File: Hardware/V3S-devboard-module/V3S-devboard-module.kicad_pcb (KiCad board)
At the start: 2 copper layers, 149.6 x 31.2 mm, 4 parts, among them CN1 AS0A826-H2RB-7H, J1 Bus_DDR4_Edge_Conn, J2 SODIMM DDR4 EDGE

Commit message: Started working in schematic
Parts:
- added U1: V3S, Package_QFP:LQFP-128_14x14mm_P0.4mm, F.Cu at (136.5, 93.5)
- added U2: EA3036C, Package_DFN_QFN:WQFN-20-1EP_3x3mm_P0.4mm_EP1.7x1.7mm, F.Cu at (171.5, 94.5)
- moved J2 248.6 mm to (329.3, 160.8)
- moved CN1 201.6 mm to (324.6, 110.2)
- moved J1 54.2 mm to (115.3, 110.8)
- moved R1 54.2 mm to (110.7, 104.6)
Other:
- board size 149.6 x 31.2 mm -> 283.6 x 80 mm
- board text removed: "LPDDR4 Testbed Rev. 1.2.0 12/2022"

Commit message: small improvements
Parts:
- added Y2: Crystal_GND23_Small, Crystal:Crystal_SMD_3225-4Pin_3.2x2.5mm, F.Cu at (121.8, 61.7)
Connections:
- J1 pad 11: unconnected-(J1-Pad11) -> LCD_D4
- U1 pad 1: unconnected-(U1-PG4/SDC1_D2/PG_EINT4-Pad1) -> /uP/PG4_SDCI_D2
- U1 pad 10: unconnected-(U1-PE20/CSI_FIELD/CSI_MIPI_MCLK-Pad10) -> /uP/PE20_MCSI_MCLK
- U1 pad 100: unconnected-(U1-PF6-Pad100) -> /uP/PF6
- U1 pad 101: unconnected-(U1-F5/SDC0_D2/JTAG_CK1-Pad101) -> /uP/PF5_SDC0D2_JTAGCK1
- U1 pad 102: unconnected-(U1-PF4/SDC0_D3/UART0_RX-Pad102) -> /uP/PF4_SDC0D3_UART0RX
- U1 pad 103: unconnected-(U1-PF3/SDC0_CMD/JTAG_DO1-Pad103) -> /uP/PF3_SDC0CMD_JTAGDO1
- U1 pad 104: unconnected-(U1-VCC-IO0-Pad104) -> VCC_IO
- U1 pad 105: unconnected-(U1-PF2/SDC0_CLK/UART0_TX-Pad105) -> /uP/PF2_SDC0CLK_UART0TX
- U1 pad 106: unconnected-(U1-PF1/SDC0_D0/JTAG_DI1-Pad106) -> /uP/PF1_SDC0D0_JTAGDI1
- U1 pad 107: unconnected-(U1-PF0/SDC0_D1/JTAG_MS1-Pad107) -> /uP/PF0_SDC0D1_JTAGDI1
- U1 pad 108: unconnected-(U1-VDD-SYS1-Pad108) -> VDD_SYS
- U1 pad 109: unconnected-(U1-VCC-USB-Pad109) -> VCC_USB
- U1 pad 11: unconnected-(U1-PE19/CSI_D15/LCD_D21-Pad11) -> LCD_D21
- U1 pad 110: unconnected-(U1-USB-DN-Pad110) -> /uP/USB_N
- U1 pad 111: unconnected-(U1-USB-DP-Pad111) -> /uP/USB_P
- U1 pad 112: unconnected-(U1-LRADC0-Pad112) -> /uP/LRADC0
- U1 pad 113: unconnected-(U1-MICIN1P-Pad113) -> /uP/MCIN1_P
- U1 pad 114: unconnected-(U1-MICIN1N-Pad114) -> /uP/MCIN1_N
- U1 pad 115: unconnected-(U1-AVCC-Pad115) -> AVCC
- U1 pad 116: unconnected-(U1-AGND-Pad116) -> GND
- U1 pad 117: unconnected-(U1-VRA1-Pad117) -> VRA1
- U1 pad 118: unconnected-(U1-VRA2-Pad118) -> VRA2
- U1 pad 119: unconnected-(U1-HBIAS-Pad119) -> /uP/HBIAS
- U1 pad 12: unconnected-(U1-VCC-PE0-Pad12) -> VCC_PE
- U1 pad 120: unconnected-(U1-HPOUTR-Pad120) -> /uP/HPOUTR
- U1 pad 121: unconnected-(U1-HPOUTL-Pad121) -> /uP/HPOUTL
- U1 pad 122: unconnected-(U1-HPVCCIN-Pad122) -> VCC_HP
- U1 pad 123: unconnected-(U1-HPVCCBP-Pad123) -> VCC_HP_BP
- U1 pad 124: unconnected-(U1-HPCOMFB-Pad124) -> /uP/HPCOMFB
- U1 pad 125: unconnected-(U1-HPCOM-Pad125) -> /uP/HPCOM
- U1 pad 126: unconnected-(U1-VDD-SYS2-Pad126) -> VDD_SYS
- U1 pad 127: unconnected-(U1-VCC-IO1-Pad127) -> VCC_IO
- U1 pad 128: unconnected-(U1-PG5/SDC1_D3/PG_EINT5-Pad128) -> /uP/PG5_SDCI_D3
- U1 pad 13: unconnected-(U1-PE18/CSI_D14/LCD_D20-Pad13) -> LCD_D20
- U1 pad 14: unconnected-(U1-PE17/CSI_D13/LCD_D19-Pad14) -> LCD_D19
- U1 pad 15: unconnected-(U1-PE16/CSI_D12/LCD_D18-Pad15) -> LCD_D18
- U1 pad 16: unconnected-(U1-PE15/CSI_D11/LCD_D15-Pad16) -> LCD_D15
- U1 pad 17: unconnected-(U1-PE14/CSI_D10/LCD_D14-Pad17) -> LCD_D14
- U1 pad 18: unconnected-(U1-PE13/CSI_D9/LCD_D13-Pad18) -> LCD_D13
- U1 pad 19: unconnected-(U1-VDD-SYS3-Pad19) -> VDD_SYS
- U1 pad 2: unconnected-(U1-PG3/SDC1_D1/PG_EINT3-Pad2) -> /uP/PG3_SDCI_D1
- U1 pad 20: unconnected-(U1-VDD-CPU3-Pad20) -> VDD_CPU
- U1 pad 21: unconnected-(U1-VDD-CPU2-Pad21) -> VDD_CPU
- U1 pad 22: unconnected-(U1-PE12/CSI_D8/LCD_D12-Pad22) -> LCD_D12
- U1 pad 23: unconnected-(U1-PE11/CSI_D7/LCD_D11-Pad23) -> LCD_D11
- U1 pad 24: unconnected-(U1-PE10/CSI_D6/LCD_D10-Pad24) -> LCD_D10
- U1 pad 25: unconnected-(U1-VDD-CPU1-Pad25) -> VDD_CPU
- U1 pad 26: unconnected-(U1-VDD-CPU0-Pad26) -> VDD_CPU
- U1 pad 27: unconnected-(U1-PE9/CSI_D5/LCD_D7-Pad27) -> LCD_D7
- U1 pad 28: unconnected-(U1-PE8/CSI_D4/LCD_D6-Pad28) -> LCD_D6
- U1 pad 29: unconnected-(U1-VCC-PE1-Pad29) -> VCC_PE
- U1 pad 3: unconnected-(U1-PG2/SDC1_D0/PG_EINT2-Pad3) -> /uP/PG2_SDCI_D0
- U1 pad 30: unconnected-(U1-PE7/CSI_D3/LCD_D5-Pad30) -> LCD_D5
- U1 pad 31: unconnected-(U1-PE6/CSI_D2/LCD_D4-Pad31) -> LCD_D4
- U1 pad 32: unconnected-(U1-PE5/CSI_D1/LCD_D3-Pad32) -> LCD_D3
- U1 pad 33: unconnected-(U1-PE4/CSI_D0/LCD_D2-Pad33) -> LCD_D2
- U1 pad 34: unconnected-(U1-PE3/CSI_VSYNC/LCD_VSYNC-Pad34) -> /uP/LCD_VSYNC
- U1 pad 35: unconnected-(U1-PE2/CSI_HSYNC/LCD_HSYNC-Pad35) -> /uP/LCD_HSYNC
- U1 pad 36: unconnected-(U1-PE1/CSI_MCLK/LCD_DE-Pad36) -> /uP/LCD_DE
- U1 pad 37: unconnected-(U1-PE0/CSI_PCLK/LCD_CLK-Pad37) -> /uP/LCD_CLK
- U1 pad 38: unconnected-(U1-VDD-CPU4-Pad38) -> VDD_CPU
- U1 pad 39: unconnected-(U1-PB0/UART2_TX/PB_EINT0-Pad39) -> /uP/PB0_UART2TX
- U1 pad 4: unconnected-(U1-PG1/SDC1_CMD/PG_EINT1-Pad4) -> /uP/PG0_MCSI_PDWN
- U1 pad 40: unconnected-(U1-PB1/UART2_RX/PB_EINT1-Pad40) -> /uP/PB1_UART2RX
- U1 pad 41: unconnected-(U1-PB2/UART2_RTS/PB_EINT2-Pad41) -> /uP/PB2_UART2RTS
- U1 pad 42: unconnected-(U1-PB3/UART2_CTS/PB_EINT3-Pad42) -> /uP/PB3_UART2CTS
- U1 pad 43: unconnected-(U1-PB4/PWM0/PB_EINT4-Pad43) -> /uP/PB4_PWM0
- U1 pad 44: unconnected-(U1-PB5/PWM1/PB_EINT5-Pad44) -> /uP/PB5_PWM1
- U1 pad 45: unconnected-(U1-PB6/TWI0_SCK/PB_EINT6-Pad45) -> /uP/PB6_SCK
- U1 pad 46: unconnected-(U1-PB7/TWI0_SDA/PB_EINT7-Pad46) -> /uP/PB7_SDA
- U1 pad 47: unconnected-(U1-VDD-CPU5-Pad47) -> VDD_CPU
- U1 pad 48: unconnected-(U1-PB8/TWI1_SCK/UART0_TX/PB_EINT8-Pad48) -> /uP/PB8_SCK_UART0TX
- U1 pad 49: unconnected-(U1-PB9/TWI1_SDA/UART0_RX/PB_EINT9-Pad49) -> /uP/PB9_SDA_UART0RX
- U1 pad 5: unconnected-(U1-PG0/SDC1_CLK/PG_EINT0-Pad5) -> /uP/PG0_MCSI_RST
- U1 pad 50: unconnected-(U1-VCC-IO3-Pad50) -> VCC_IO
- U1 pad 51: unconnected-(U1-VDD-CPU6-Pad51) -> VDD_CPU
- U1 pad 52: unconnected-(U1-PC0/SDC2_CLK/SPI_MISO-Pad52) -> /uP/PC0_SPI_MISO
- U1 pad 53: unconnected-(U1-PC1/SDC2_CMD/SPI_CLK-Pad53) -> /uP/PC1_SPI_CLK
- U1 pad 54: unconnected-(U1-PC2/SDC2_RST/SPI_CS-Pad54) -> /uP/PC2_SPI_CS
- U1 pad 55: unconnected-(U1-PC3/SDC2_D0/SPI_MOSI-Pad55) -> /uP/PC3_SPI_MOSI
- U1 pad 56: unconnected-(U1-VDD-CPU7-Pad56) -> VDD_CPU
- U1 pad 57: unconnected-(U1-VCC-IO2-Pad57) -> VCC_IO
- U1 pad 58: unconnected-(U1-VDD-SYS4-Pad58) -> VDD_SYS
- U1 pad 59: unconnected-(U1-VCC-DRAM8-Pad59) -> VCC_DRAM
- U1 pad 6: unconnected-(U1-PE24/LCD_D23-Pad6) -> LCD_D23
- U1 pad 60: unconnected-(U1-VCC-DRAM9-Pad60) -> VCC_DRAM
- U1 pad 61: unconnected-(U1-VCC-DRAM10-Pad61) -> VCC_DRAM
- U1 pad 62: unconnected-(U1-VCC-DARM11-Pad62) -> VCC_DRAM
- U1 pad 63: unconnected-(U1-SVREF1-Pad63) -> SVREF
- U1 pad 64: unconnected-(U1-VDD-SYS5-Pad64) -> VDD_SYS
- U1 pad 65: unconnected-(U1-VCC-DRAM0-Pad65) -> VCC_DRAM
- U1 pad 66: unconnected-(U1-VCC-DRAM1-Pad66) -> VCC_DRAM
- U1 pad 67: unconnected-(U1-VCC-DRAM2-Pad67) -> VCC_DRAM
- U1 pad 68: unconnected-(U1-VCC-DRAM3-Pad68) -> VCC_DRAM
- U1 pad 69: unconnected-(U1-VCC-DRAM4-Pad69) -> VCC_DRAM
- U1 pad 7: unconnected-(U1-PE23/LCD_D22-Pad7) -> LCD_D22
- U1 pad 70: unconnected-(U1-VCC-DRAM5-Pad70) -> VCC_DRAM
- U1 pad 71: unconnected-(U1-SVREF0-Pad71) -> SVREF
- U1 pad 72: unconnected-(U1-VCC-DRAM6-Pad72) -> VCC_DRAM
- U1 pad 73: unconnected-(U1-SZQ-Pad73) -> /uP/SZQ
- U1 pad 74: unconnected-(U1-X24MOUT-Pad74) -> /uP/X24MOUT
- U1 pad 75: unconnected-(U1-X24MIN-Pad75) -> /uP/X24_MIN
- U1 pad 76: unconnected-(U1-VCC-PLL-Pad76) -> VCC_PLL
- U1 pad 77: unconnected-(U1-EPHY-LINK-LED-Pad77) -> /uP/ETH_LED_LINK
- U1 pad 78: unconnected-(U1-EPHY-SPD-LED-Pad78) -> /uP/ETH_LED_SPD
- U1 pad 79: unconnected-(U1-VCC-DRAM7-Pad79) -> VCC_DRAM
- U1 pad 8: unconnected-(U1-PE22/CSI_SDA/TWI1_SDA/UART1_RX-Pad8) -> /uP/PE22_CSI_SDA
- U1 pad 80: unconnected-(U1-VDD-SYS0-Pad80) -> VDD_SYS
- U1 pad 81: unconnected-(U1-MCSI-D0P-Pad81) -> /uP/MSCI_D0_P
- U1 pad 82: unconnected-(U1-MCSI-D0N-Pad82) -> /uP/MSCI_D0_N
- U1 pad 83: unconnected-(U1-MCSI-D1P-Pad83) -> /uP/MSCI_D1_P
- U1 pad 84: unconnected-(U1-MCSI-D1N-Pad84) -> /uP/MSCI_D1_N
- U1 pad 85: unconnected-(U1-VCC-MCSI-Pad85) -> VCC_MSCI
- U1 pad 86: unconnected-(U1-MCSI-CKP-Pad86) -> /uP/MSCI_CLK_P
- U1 pad 87: unconnected-(U1-MCSI-CKN-Pad87) -> /uP/MSCI_CLK_N
- U1 pad 88: unconnected-(U1-EPHY-VDD-Pad88) -> VDD_PHY
- U1 pad 89: unconnected-(U1-EPHY-RXN-Pad89) -> ETH0.RX_N
- U1 pad 9: unconnected-(U1-PE21/CSI_SCK/TWI1_SCK/UART1_TX-Pad9) -> /uP/PE21_CSI_SCK
- U1 pad 90: unconnected-(U1-EPHY-RXP-Pad90) -> ETH0.RX_P
- U1 pad 91: unconnected-(U1-EPHY-TXN-Pad91) -> ETH0.TX_N
- U1 pad 92: unconnected-(U1-EPHY-TXP-Pad92) -> ETH0.TX_P
- U1 pad 93: unconnected-(U1-EPHY-VCC-Pad93) -> VCC_PHY
- U1 pad 94: unconnected-(U1-EPHY-RTX-Pad94) -> Net-(U1-EPHY-RTX)
- U1 pad 95: unconnected-(U1-X32KOUT-Pad95) -> /uP/X32KOUT
- U1 pad 96: unconnected-(U1-X32KIN-Pad96) -> /uP/X32KIN
- U1 pad 97: unconnected-(U1-RTC-VIO-Pad97) -> VCC_RTCIO
- U1 pad 98: unconnected-(U1-VCC-RTC-Pad98) -> VCC_RTC
- U1 pad 99: unconnected-(U1-RESET-Pad99) -> /uP/RESET

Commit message: schematic improvements
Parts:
- added REF**: CONN-SMD_AS0BC21-S30BE-7H, v3s-devboard-module:CONN-SMD_AS0BC21-S30BE-7H, F.Cu at (33.1, 167.9)
- added REF**: m2-padKeyE, v3s-devboard-module:m2-padKeyE, B.Cu at (64.7, 184.9)
- added U$3: M.2-B-KEY-2280-ADAPTER, M.2-Templates:M.2-B-KEY-2280-ADAPTER, F.Cu at (222.9, 152.2)
- moved U1 113.1 mm to (34.1, 141.5), turned to 45 degrees
- moved U2 1.33 mm to (171.2, 93.2)

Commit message: general improvements. power almost complete
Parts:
- removed CN1: AS0A826-H2RB-7H, SODIMM:SODIMM_DDR4_EDGE
- removed R1: R_US, Resistor_SMD:R_0402_1005Metric_Pad0.72x0.64mm_HandSolder
- removed U$3: M.2-B-KEY-2280-ADAPTER, M.2-Templates:M.2-B-KEY-2280-ADAPTER
- added CN3: AS0BC21-S30BE-7H, v3s-devboard-module:m2-padKeyE, F.Cu at (89.8, 102.9)
- added RN1: 6x47K, Resistor_THT:R_Array_SIP7, F.Cu at (36.5, 97.5)
- added U3: XC6206PxxxMR, Package_TO_SOT_SMD:SOT-23-3, F.Cu at (58.5, 97.7)
- added U4: W25Q128JVS, Package_SO:SOIC-8_5.23x5.23mm_P1.27mm, F.Cu at (39.4, 119.4)
- added U5: AP3019AKTR-G1, Package_TO_SOT_SMD:SOT-23-6, F.Cu at (47.2, 118.4)
- J2: value SODIMM DDR4 EDGE -> Micro_SD_Card_Det1; footprint SODIMM:SODIMM_DDR4_EDGE -> v3s-devboard-module:J_sd_micro_socket
- U1: footprint Package_QFP:LQFP-128_14x14mm_P0.4mm -> v3s-devboard-module:LQFP-128_L14.0-W14.0-P0.40-LS16.0-BL-EP5.0
- moved J2 290.2 mm to (44.1, 107.7)
- moved U1 99.7 mm to (123.4, 97.2)
- moved REF** 88.6 mm to (89.8, 99.8)
- moved J1 86.1 mm to (32.2, 88.4)
- moved REF** 84.0 mm to (121.0, 122.6)
- moved U2 55.3 mm to (118.2, 77.6)
- moved Y2 16.8 mm to (128.1, 77.2)
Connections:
- net VCC_DRAM renamed 1V8
- J2 pad 1: (no net) -> /uP/PF5_SDC0D2_JTAGCK1
- J2 pad 2: (no net) -> /uP/PF4_SDC0D3_UART0RX
- J2 pad 3: (no net) -> /uP/PF3_SDC0CMD_JTAGDO1
- J2 pad 4: (no net) -> 3V3
- J2 pad 5: (no net) -> /uP/PF2_SDC0CLK_UART0TX
- J2 pad 6: (no net) -> GND
- J2 pad 7: (no net) -> /uP/PF1_SDC0D0_JTAGDI1
- J2 pad 8: (no net) -> /uP/PF0_SDC0D1_JTAGDI1
- J2 pad 9: (no net) -> /uP/PF6
- U1 pad 10: /uP/PE20_MCSI_MCLK -> CSI.MCSI_MCLK
- U1 pad 104: VCC_IO -> 3V3
- U1 pad 108: VDD_SYS -> 1V2
- U1 pad 109: VCC_USB -> 3V3
- U1 pad 115: AVCC -> 3V0
- U1 pad 12: VCC_PE -> 3V3
- U1 pad 122: VCC_HP -> 3V3
- U1 pad 126: VDD_SYS -> 1V2
- U1 pad 127: VCC_IO -> 3V3
- U1 pad 19: VDD_SYS -> 1V2
- U1 pad 20: VDD_CPU -> 1V2
- U1 pad 21: VDD_CPU -> 1V2
- U1 pad 25: VDD_CPU -> 1V2
- U1 pad 26: VDD_CPU -> 1V2
- U1 pad 29: VCC_PE -> 3V3
- U1 pad 34: /uP/LCD_VSYNC -> LCD0.VSYNC
- U1 pad 35: /uP/LCD_HSYNC -> LCD0.HSYNC
- U1 pad 36: /uP/LCD_DE -> LCD0.DE
- U1 pad 37: /uP/LCD_CLK -> LCD0.CLK
- U1 pad 38: VDD_CPU -> 1V2
- U1 pad 39: /uP/PB0_UART2TX -> UART2.TX
- U1 pad 40: /uP/PB1_UART2RX -> UART2.RX
- U1 pad 41: /uP/PB2_UART2RTS -> /uP/PB2
- U1 pad 42: /uP/PB3_UART2CTS -> UART2.CTS
- U1 pad 47: VDD_CPU -> 1V2
- U1 pad 48: /uP/PB8_SCK_UART0TX -> UART0.TX
- U1 pad 49: /uP/PB9_SDA_UART0RX -> UART0.RX
- U1 pad 50: VCC_IO -> 3V3
- U1 pad 51: VDD_CPU -> 1V2
- U1 pad 52: /uP/PC0_SPI_MISO -> SPI.MISO
- U1 pad 53: /uP/PC1_SPI_CLK -> SPI.CLK
- U1 pad 54: /uP/PC2_SPI_CS -> SPI.CS
- U1 pad 55: /uP/PC3_SPI_MOSI -> SPI.MOSI
- U1 pad 56: VDD_CPU -> 1V2
- U1 pad 57: VCC_IO -> 3V3
- U1 pad 58: VDD_SYS -> 1V2
- U1 pad 64: VDD_SYS -> 1V2
- U1 pad 76: VCC_PLL -> 3V0
- U1 pad 77: /uP/ETH_LED_LINK -> ETH_LED_LINK
- U1 pad 78: /uP/ETH_LED_SPD -> ETH_LED_SPD
- U1 pad 8: /uP/PE22_CSI_SDA -> CSI.CSI_SDA
- U1 pad 80: VDD_SYS -> 1V2
- U1 pad 81: /uP/MSCI_D0_P -> CSI.MCSI_D0_P
- U1 pad 82: /uP/MSCI_D0_N -> CSI.MCSI_D0_N
- U1 pad 83: /uP/MSCI_D1_P -> CSI.MCSI_D1_P
- U1 pad 84: /uP/MSCI_D1_N -> CSI.MCSI_D1_N
- U1 pad 85: VCC_MSCI -> 3V3
- U1 pad 86: /uP/MSCI_CLK_P -> CSI.MCSI_CK_P
- U1 pad 87: /uP/MSCI_CLK_N -> CSI.MCSI_CK_N
- U1 pad 88: VDD_PHY -> 1V2
- U1 pad 9: /uP/PE21_CSI_SCK -> CSI.CSI_SCK
- U1 pad 93: VCC_PHY -> 3V3
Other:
- board size 283.6 x 80 mm -> 69.6 x 26 mm

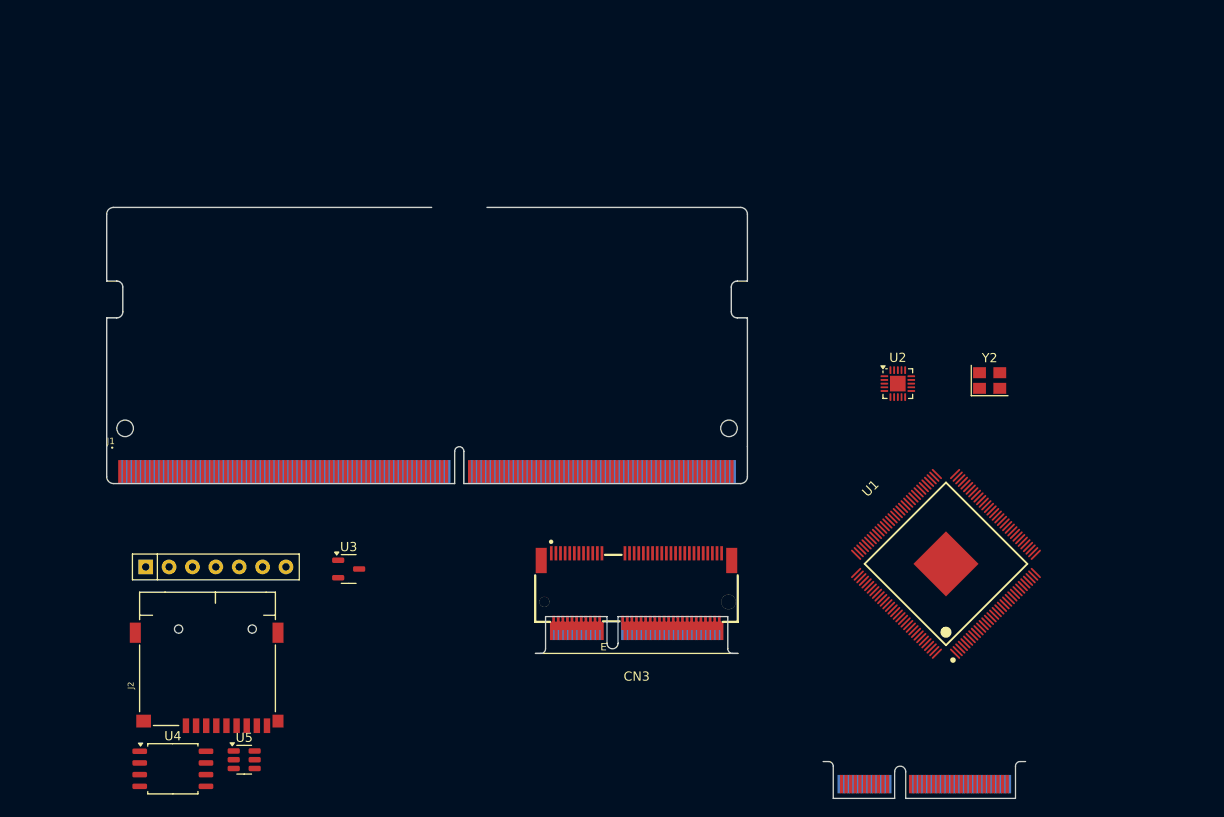
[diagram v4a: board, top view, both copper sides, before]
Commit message: fixed minor schematic issues
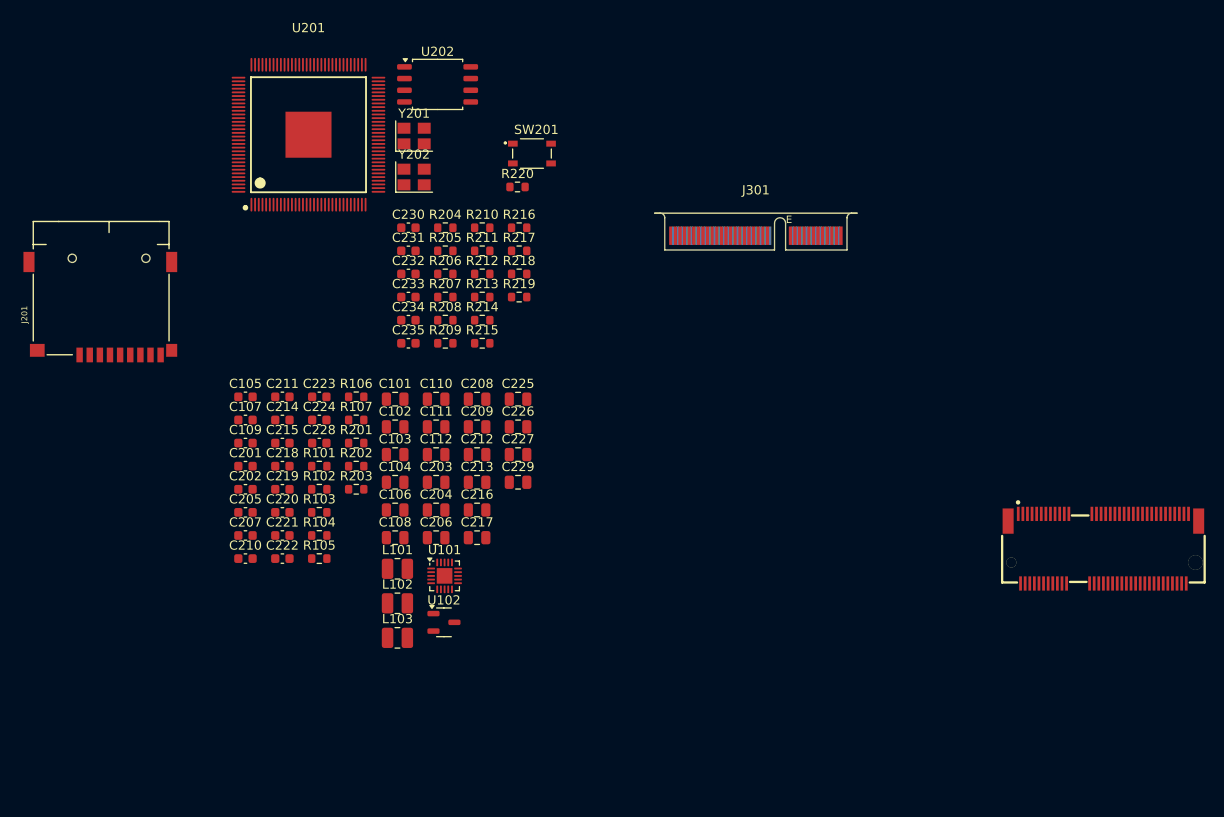
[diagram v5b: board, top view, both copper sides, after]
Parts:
- removed CN3: AS0BC21-S30BE-7H, v3s-devboard-module:m2-padKeyE
- removed J1: Bus_DDR4_Edge_Conn, SODIMM-DDR4:Bus_DDR4_Conn_Edge
- removed J2: Micro_SD_Card_Det1, v3s-devboard-module:J_sd_micro_socket
- removed the REF** at (121.0, 122.6)
- removed RN1: 6x47K, Resistor_THT:R_Array_SIP7
- removed U1: V3S, v3s-devboard-module:LQFP-128_L14.0-W14.0-P0.40-LS16.0-BL-EP5.0
- removed U2: EA3036C, Package_DFN_QFN:WQFN-20-1EP_3x3mm_P0.4mm_EP1.7x1.7mm
- removed U3: XC6206PxxxMR, Package_TO_SOT_SMD:SOT-23-3
- removed U4: W25Q128JVS, Package_SO:SOIC-8_5.23x5.23mm_P1.27mm
- removed U5: AP3019AKTR-G1, Package_TO_SOT_SMD:SOT-23-6
- removed Y2: Crystal_GND23_Small, Crystal:Crystal_SMD_3225-4Pin_3.2x2.5mm
- added C101: 1u, Capacitor_SMD:C_0805_2012Metric, F.Cu at (63.6, 79.3)
- added C102: 10u, Capacitor_SMD:C_0805_2012Metric, F.Cu at (63.6, 82.3)
- added C103: 10u, Capacitor_SMD:C_0805_2012Metric, F.Cu at (63.6, 85.3)
- added C104: 10u, Capacitor_SMD:C_0805_2012Metric, F.Cu at (63.6, 88.3)
- added C105: 18p, Capacitor_SMD:C_0603_1608Metric, F.Cu at (47.3, 79.0)
- added C106: 10u, Capacitor_SMD:C_0805_2012Metric, F.Cu at (63.6, 91.3)
- added C107: 18p, Capacitor_SMD:C_0603_1608Metric, F.Cu at (47.3, 81.5)
- added C108: 10u, Capacitor_SMD:C_0805_2012Metric, F.Cu at (63.6, 94.3)
- added C109: 18p, Capacitor_SMD:C_0603_1608Metric, F.Cu at (47.3, 84.0)
- added C110: 10u, Capacitor_SMD:C_0805_2012Metric, F.Cu at (68.0, 79.3)
- added C111: 1u, Capacitor_SMD:C_0805_2012Metric, F.Cu at (68.0, 82.3)
- added C112: 1u, Capacitor_SMD:C_0805_2012Metric, F.Cu at (68.0, 85.3)
- added C201: 100n, Capacitor_SMD:C_0603_1608Metric, F.Cu at (47.3, 86.5)
- added C202: 100n, Capacitor_SMD:C_0603_1608Metric, F.Cu at (47.3, 89.0)
- added C203: 10u, Capacitor_SMD:C_0805_2012Metric, F.Cu at (68.0, 88.3)
- added C204: 1u, Capacitor_SMD:C_0805_2012Metric, F.Cu at (68.0, 91.3)
- added C205: 100n, Capacitor_SMD:C_0603_1608Metric, F.Cu at (47.3, 91.6)
- added C206: 1u, Capacitor_SMD:C_0805_2012Metric, F.Cu at (68.0, 94.3)
- added C207: 100n, Capacitor_SMD:C_0603_1608Metric, F.Cu at (47.3, 94.1)
- added C208: 10u, Capacitor_SMD:C_0805_2012Metric, F.Cu at (72.5, 79.3)
- added C209: 1u, Capacitor_SMD:C_0805_2012Metric, F.Cu at (72.5, 82.3)
- added C210: 100n, Capacitor_SMD:C_0603_1608Metric, F.Cu at (47.3, 96.6)
- added C211: 100n, Capacitor_SMD:C_0603_1608Metric, F.Cu at (51.3, 79.0)
- added C212: 10u, Capacitor_SMD:C_0805_2012Metric, F.Cu at (72.5, 85.3)
- added C213: 1u, Capacitor_SMD:C_0805_2012Metric, F.Cu at (72.5, 88.3)
- added C214: 100n, Capacitor_SMD:C_0603_1608Metric, F.Cu at (51.3, 81.5)
- added C215: 100n, Capacitor_SMD:C_0603_1608Metric, F.Cu at (51.3, 84.0)
- added C216: 10u, Capacitor_SMD:C_0805_2012Metric, F.Cu at (72.5, 91.3)
- added C217: 1u, Capacitor_SMD:C_0805_2012Metric, F.Cu at (72.5, 94.3)
- added C218: 100n, Capacitor_SMD:C_0603_1608Metric, F.Cu at (51.3, 86.5)
- added C219: 100n, Capacitor_SMD:C_0603_1608Metric, F.Cu at (51.3, 89.0)
- added C220: 100n, Capacitor_SMD:C_0603_1608Metric, F.Cu at (51.3, 91.6)
- added C221: 100n, Capacitor_SMD:C_0603_1608Metric, F.Cu at (51.3, 94.1)
- added C222: 100n, Capacitor_SMD:C_0603_1608Metric, F.Cu at (51.3, 96.6)
- added C223: 100n, Capacitor_SMD:C_0603_1608Metric, F.Cu at (55.3, 79.0)
- added C224: 100n, Capacitor_SMD:C_0603_1608Metric, F.Cu at (55.3, 81.5)
- added C225: 1u, Capacitor_SMD:C_0805_2012Metric, F.Cu at (76.9, 79.3)
- added C226: 4.7u, Capacitor_SMD:C_0805_2012Metric, F.Cu at (76.9, 82.3)
- added C227: 10u, Capacitor_SMD:C_0805_2012Metric, F.Cu at (76.9, 85.3)
- added C228: 100n, Capacitor_SMD:C_0603_1608Metric, F.Cu at (55.3, 84.0)
- added C229: 4.7u, Capacitor_SMD:C_0805_2012Metric, F.Cu at (76.9, 88.3)
- added C230: 18p, Capacitor_SMD:C_0603_1608Metric, F.Cu at (65.0, 60.6)
- added C231: 18p, Capacitor_SMD:C_0603_1608Metric, F.Cu at (65.0, 63.1)
- added C232: 18p, Capacitor_SMD:C_0603_1608Metric, F.Cu at (65.0, 65.7)
- added C233: 18p, Capacitor_SMD:C_0603_1608Metric, F.Cu at (65.0, 68.2)
- added C234: 1u, Capacitor_SMD:C_0603_1608Metric, F.Cu at (65.0, 70.7)
- added C235: 100n, Capacitor_SMD:C_0603_1608Metric, F.Cu at (65.0, 73.2)
- added J201: Micro_SD_Card_Det1, v3s-devboard-module:J_sd_micro_socket, F.Cu at (32.5, 67.4)
- added J301: AS0BC21-S30BE-7H, v3s-devboard-module:m2-padKeyE, F.Cu at (102.8, 63.0)
- added L101: 2.2u, Inductor_SMD:L_1008_2520Metric, F.Cu at (63.8, 97.7)
- added L102: 2.2u, Inductor_SMD:L_1008_2520Metric, F.Cu at (63.8, 101.4)
- added L103: 2.2u, Inductor_SMD:L_1008_2520Metric, F.Cu at (63.8, 105.2)
- added R101: 150K, Resistor_SMD:R_0603_1608Metric, F.Cu at (55.3, 86.5)
- added R102: 150K, Resistor_SMD:R_0603_1608Metric, F.Cu at (55.3, 89.0)
- added R103: 200K, Resistor_SMD:R_0603_1608Metric, F.Cu at (55.3, 91.6)
- added R104: 100K, Resistor_SMD:R_0603_1608Metric, F.Cu at (55.3, 94.1)
- added R105: 680K, Resistor_SMD:R_0603_1608Metric, F.Cu at (55.3, 96.6)
- added R106: 150K, Resistor_SMD:R_0603_1608Metric, F.Cu at (59.3, 79.0)
- added R107: 0, Resistor_SMD:R_0603_1608Metric, F.Cu at (59.3, 81.5)
- added R201: 2K, Resistor_SMD:R_0603_1608Metric, F.Cu at (59.3, 84.0)
- added R202: 2K, Resistor_SMD:R_0603_1608Metric, F.Cu at (59.3, 86.5)
- added R203: 200K, Resistor_SMD:R_0603_1608Metric, F.Cu at (59.3, 89.0)
- added R204: 10M, Resistor_SMD:R_0603_1608Metric, F.Cu at (69.0, 60.6)
- added R205: 10M, Resistor_SMD:R_0603_1608Metric, F.Cu at (69.0, 63.1)
- added R206: 240, Resistor_SMD:R_0603_1608Metric, F.Cu at (69.0, 65.7)
- added R207: 47K, Resistor_SMD:R_0603_1608Metric, F.Cu at (69.0, 68.2)
- added R208: 10K, Resistor_SMD:R_0603_1608Metric, F.Cu at (69.0, 70.7)
- added R209: 33, Resistor_SMD:R_0603_1608Metric, F.Cu at (69.0, 73.2)
- added R210: 47K, Resistor_SMD:R_0603_1608Metric, F.Cu at (73.0, 60.6)
- added R211: 10k, Resistor_SMD:R_0603_1608Metric, F.Cu at (73.0, 63.1)
- added R212: 10k, Resistor_SMD:R_0603_1608Metric, F.Cu at (73.0, 65.7)
- added R213: 10k, Resistor_SMD:R_0603_1608Metric, F.Cu at (73.0, 68.2)
- added R214: 10k, Resistor_SMD:R_0603_1608Metric, F.Cu at (73.0, 70.7)
- added R215: 10k, Resistor_SMD:R_0603_1608Metric, F.Cu at (73.0, 73.2)
- added R216: 33, Resistor_SMD:R_0603_1608Metric, F.Cu at (77.0, 60.6)
- added R217: 33, Resistor_SMD:R_0603_1608Metric, F.Cu at (77.0, 63.1)
- added R218: 33, Resistor_SMD:R_0603_1608Metric, F.Cu at (77.0, 65.7)
- added R219: 33, Resistor_SMD:R_0603_1608Metric, F.Cu at (77.0, 68.2)
- added R220: 6K, Resistor_SMD:R_0603_1608Metric, F.Cu at (76.9, 56.2)
- added SW201: SW_MEC_5E, v3s-devboard-module:SW_SKRPACE010, F.Cu at (78.4, 52.6)
- added U101: EA3036C, Package_DFN_QFN:WQFN-20-1EP_3x3mm_P0.4mm_EP1.7x1.7mm, F.Cu at (68.9, 98.5)
- added U102: XC6206PxxxMR, Package_TO_SOT_SMD:SOT-23-3, F.Cu at (68.9, 103.5)
- added U201: V3S, v3s-devboard-module:LQFP-128_L14.0-W14.0-P0.40-LS16.0-BL-EP5.0, F.Cu at (54.1, 50.5)
- added U202: W25Q128JVS, Package_SO:SOIC-8_5.23x5.23mm_P1.27mm, F.Cu at (68.2, 45.1)
- added Y201: Crystal_GND23_Small, Crystal:Crystal_SMD_3225-4Pin_3.2x2.5mm, F.Cu at (65.6, 50.7)
- added Y202: Crystal_GND23_Small, Crystal:Crystal_SMD_3225-4Pin_3.2x2.5mm, F.Cu at (65.6, 55.1)
- moved REF** 50.9 mm to (140.5, 95.5)
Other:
- board size 69.6 x 26 mm -> 22 x 4 mm

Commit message: started preparing layout
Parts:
- C220, C221, C227, C228: moved to B.Cu
- moved C202 137.3 mm to (168.5, 24.5), turned to 90 degrees
- moved C201 133.9 mm to (166.0, 24.5), turned to 90 degrees
- moved C207 132.2 mm to (159.3, 23.8)
- moved C210 131.1 mm to (173.7, 62.0)
- moved C205 128.4 mm to (159.4, 29.0)
- moved R202 123.9 mm to (168.5, 28.0), turned to 90 degrees
- moved C211 123.0 mm to (173.7, 66.5)
- moved C218 122.9 mm to (164.0, 37.5)
- moved C219 122.9 mm to (164.0, 40.0)
- moved R201 121.4 mm to (167.0, 28.0), turned to 90 degrees
- moved C220 120.7 mm to (158.8, 36.5), turned to 180 degrees
- moved C206 116.6 mm to (159.5, 22.0)
- moved C204 111.8 mm to (159.4, 27.0)
- moved C221 111.6 mm to (153.0, 48.0), turned to 90 degrees
- moved C216 110.5 mm to (169.0, 37.5)
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
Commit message: layout improvements.
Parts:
- added NT1: NetTie_2, NetTie:NetTie-2_SMD_Pad2.0mm, F.Cu at (160.1, 17.5)
- C101, C102, C103, C104, C106, C108, C110, C111, C112, C203, C204, C206, C208, C209, C212, C213, C216, C217, C225, C226, C227, C229: footprint Capacitor_SMD:C_0805_2012Metric -> Capacitor_SMD:C_0603_1608Metric
- C105, C107, C109, C202, C205, C207, C210, C211, C214, C215, C218, C219, C220, C221, C222, C223, C224, C228: footprint Capacitor_SMD:C_0603_1608Metric -> Capacitor_SMD:C_0402_1005Metric
- R101, R102, R103, R104, R105, R106, R201, R202, R203: footprint Resistor_SMD:R_0603_1608Metric -> Resistor_SMD:R_0402_1005Metric
- moved C105 138.7 mm to (225.6, 88.2)
- moved C101 138.0 mm to (223.2, 85.2), turned to 90 degrees
- moved C103 137.5 mm to (222.3, 93.4), turned to -90 degrees
- moved C104 135.2 mm to (220.5, 93.4), turned to -90 degrees
- moved C102 135.1 mm to (220.9, 84.9), turned to 90 degrees
- moved R102 134.2 mm to (227.6, 88.2)
- moved R101 132.4 mm to (225.6, 87.2), turned to 180 degrees
- moved C106 131.2 mm to (229.5, 89.0), turned to -90 degrees
- moved U101 130.8 mm to (221.3, 89.2)
- moved C107 129.0 mm to (215.7, 91.2), turned to 90 degrees
- moved C109 128.1 mm to (215.7, 85.1), turned to 90 degrees
- moved L101 127.4 mm to (226.5, 90.2)
- moved R106 122.6 mm to (215.7, 87.0), turned to -90 degrees
- moved R104 122.4 mm to (215.7, 93.2), turned to -90 degrees
- moved R103 121.3 mm to (214.6, 91.2), turned to -90 degrees
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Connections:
- C203 pad 2: 1V8 -> VCC_DRAM
- C204 pad 2: 1V8 -> VCC_DRAM
- C205 pad 2: 1V8 -> VCC_DRAM
- C206 pad 2: 1V8 -> VCC_DRAM
- C207 pad 2: 1V8 -> VCC_DRAM
- R201 pad 1: 1V8 -> VCC_DRAM
- U201 pad 59: 1V8 -> VCC_DRAM
- U201 pad 60: 1V8 -> VCC_DRAM
- U201 pad 61: 1V8 -> VCC_DRAM
- U201 pad 62: 1V8 -> VCC_DRAM
- U201 pad 65: 1V8 -> VCC_DRAM
- U201 pad 66: 1V8 -> VCC_DRAM
- U201 pad 67: 1V8 -> VCC_DRAM
- U201 pad 68: 1V8 -> VCC_DRAM
- U201 pad 69: 1V8 -> VCC_DRAM
- U201 pad 70: 1V8 -> VCC_DRAM
- U201 pad 72: 1V8 -> VCC_DRAM
- U201 pad 79: 1V8 -> VCC_DRAM
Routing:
- net VCC_DRAM: track 0.00 -> 39.7 mm
- net 5V: track 0.00 -> 11.9 mm
